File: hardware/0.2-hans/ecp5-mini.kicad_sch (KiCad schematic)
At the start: 28 parts, among them J3 S7 Mini, J4 S7 Mini, U2 ECP5U_25_CABGA256, X1 16MHz

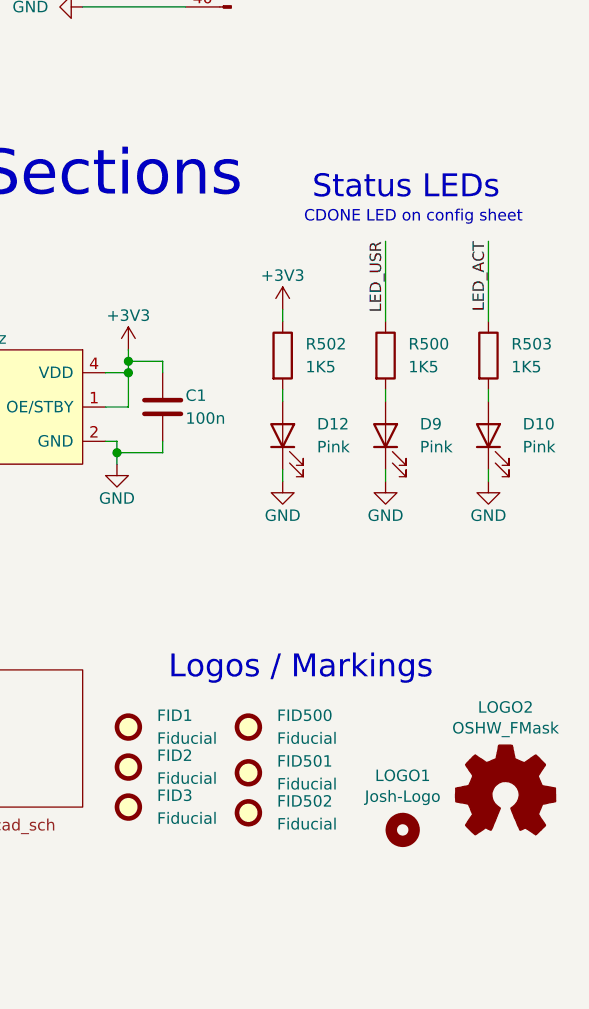
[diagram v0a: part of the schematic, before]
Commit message: remove usb, add 5v
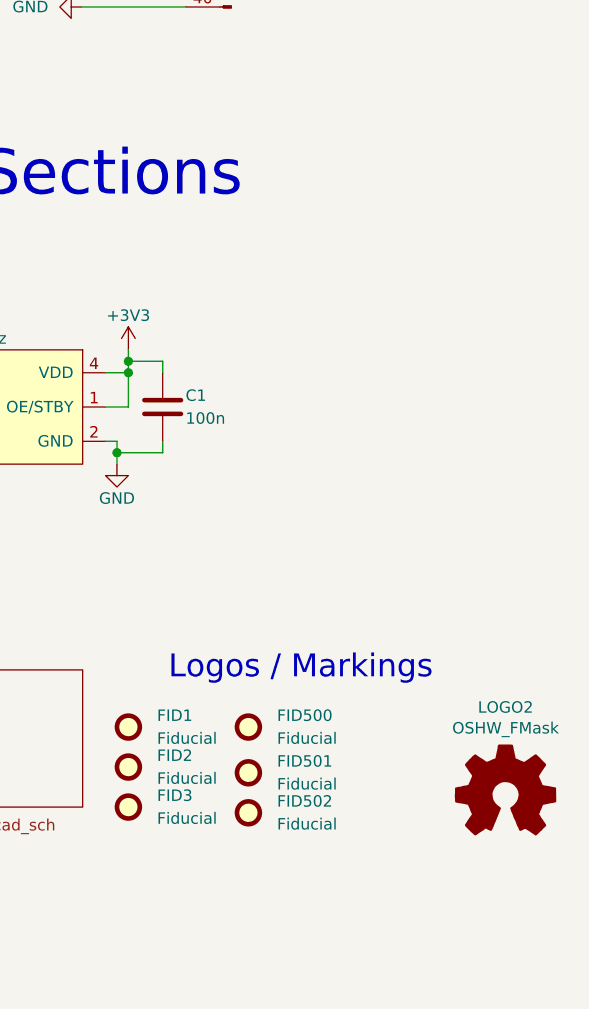
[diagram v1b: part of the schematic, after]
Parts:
- removed D10, D12, D9: Pink, LED_SMD:LED_0603_1608Metric, symbol Device:LED
- removed LOGO1: Josh-Logo, josh-logos:josh-johnson-logo-8_6x1_5, symbol Mechanical:MountingHole
- removed R500, R502, R503: 1K5, Resistor_SMD:R_0402_1005Metric, symbol Device:R
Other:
- note removed: "CDONE LED on config sheet"
- note removed: "Status LEDs"
